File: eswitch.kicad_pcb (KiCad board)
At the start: 4 copper layers, 181 x 57.5 mm, 160 parts, among them J1 691218410002, J10 691218410002, J11 691218410002, J12 691218410002, J2 +12V IN, J3 GND IN, J4 USB-C, J5 UART, J6 691218410002, J7 691218410002, J8 691218410002, J9 691218410002, SW1 RESET, SW2 BOOT, U1 BTS7004-1EPP, U10 ESP32-S3-WROOM-1-N8, U11 SRV05-4HTG-D, U2 BTS7004-1EPP, U3 BTS7008-1EPR, U4 BTS7008-1EPR, U5 BTS7008-1EPR, U6 BTS7008-1EPR, U7 BTS7008-1EPR, U8 BTS7002-1EPP, U9 TPS54360B

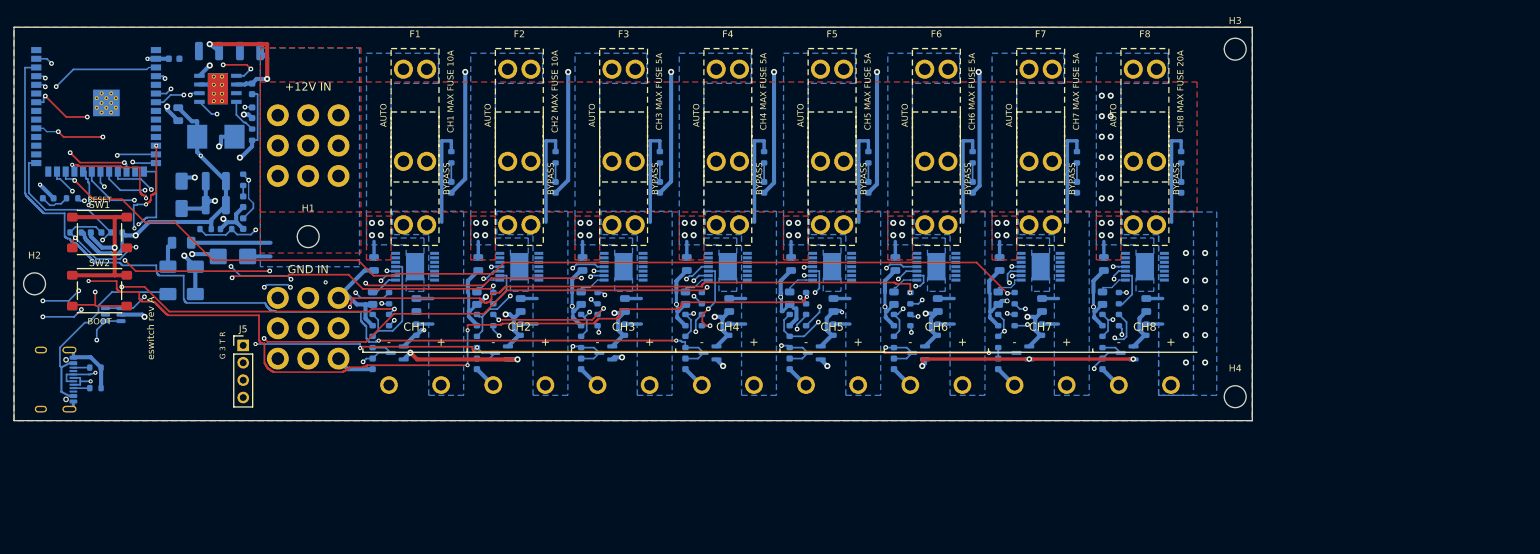
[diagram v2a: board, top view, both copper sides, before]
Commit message: Checkpoint unfinished revision B power protection and PCB review
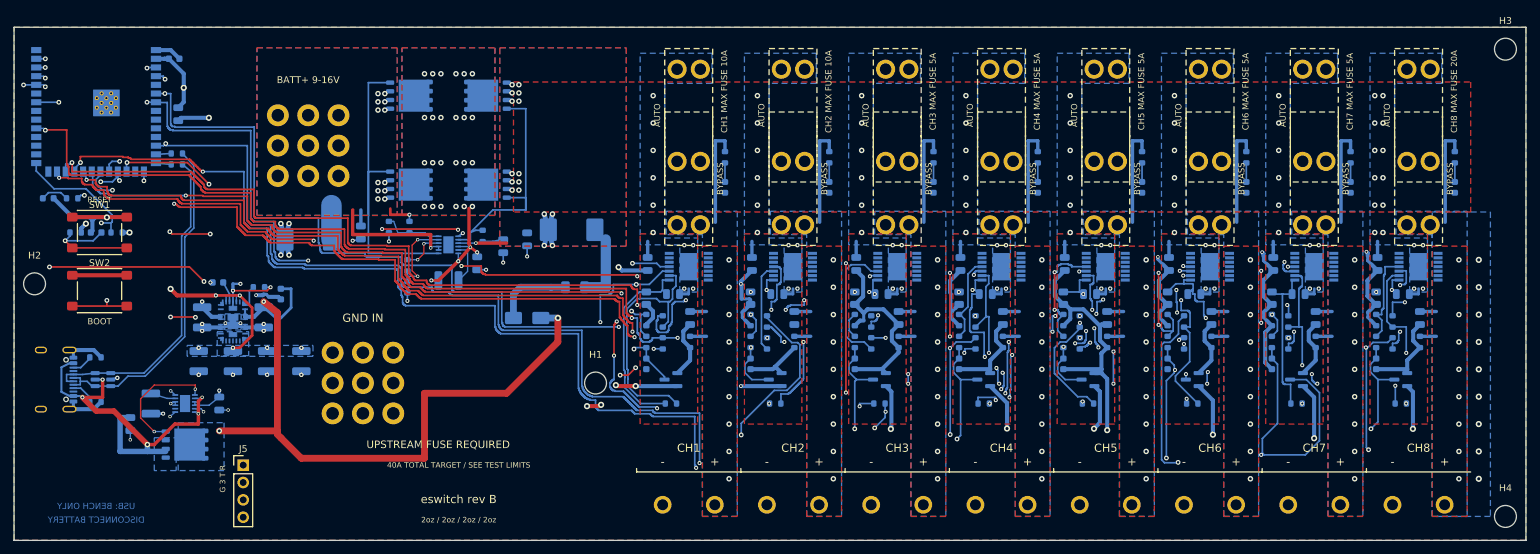
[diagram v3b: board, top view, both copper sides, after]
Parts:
- removed C4: 100nF 25V, Capacitor_SMD:C_0603_1608Metric
- removed C5: 27nF, Capacitor_SMD:C_0603_1608Metric
- removed C6: 150pF, Capacitor_SMD:C_0603_1608Metric
- removed D2, D4: B360A, Diode_SMD:D_SMA
- removed L1: 10uH 4A, Inductor_SMD:L_Bourns_SRP7028A_7.3x6.6mm
- removed R2: 31.6k 1%, Resistor_SMD:R_0603_1608Metric
- removed R3: 10.2k 1%, Resistor_SMD:R_0603_1608Metric
- removed R4: 3.9k, Resistor_SMD:R_0603_1608Metric
- added C104: 47nF 50V, Capacitor_SMD:C_0805_2012Metric, B.Cu at (96.3, 39.0)
- added C12: 22uF 10V, Capacitor_SMD:C_1210_3225Metric, B.Cu at (37.0, 48.8)
- added C13: 22uF 10V, Capacitor_SMD:C_1210_3225Metric, B.Cu at (42.0, 48.8)
- added C14: 1uF, Capacitor_SMD:C_0603_1608Metric, B.Cu at (29.8, 37.3)
- added C15: 100nF 50V, Capacitor_SMD:C_0805_2012Metric, B.Cu at (50.7, 30.0)
- added C16: 100nF 50V, Capacitor_SMD:C_0805_2012Metric, B.Cu at (67.7, 34.5)
- added C17: 4.7uF 50V, Capacitor_SMD:C_1210_3225Metric, B.Cu at (63.5, 37.0)
- added C18: 10nF 50V, Capacitor_SMD:C_0805_2012Metric, B.Cu at (71.5, 32.0)
- added C19: 100nF 50V, Capacitor_SMD:C_0805_2012Metric, B.Cu at (75.0, 31.0)
- added C20: 100nF 50V, Capacitor_SMD:C_0805_2012Metric, B.Cu at (17.0, 58.0)
- added C204: 47nF 50V, Capacitor_SMD:C_0805_2012Metric, B.Cu at (111.6, 39.0)
- added C21: 100nF 50V, Capacitor_SMD:C_0805_2012Metric, B.Cu at (30.0, 55.0)
- added C22: 4.7uF 50V, Capacitor_SMD:C_1210_3225Metric, B.Cu at (20.0, 55.0)
- added C304: 47nF 50V, Capacitor_SMD:C_0805_2012Metric, B.Cu at (126.8, 39.0)
- added C404: 47nF 50V, Capacitor_SMD:C_0805_2012Metric, B.Cu at (142.0, 39.0)
- added C504: 47nF 50V, Capacitor_SMD:C_0805_2012Metric, B.Cu at (157.3, 39.0)
- added C604: 47nF 50V, Capacitor_SMD:C_0805_2012Metric, B.Cu at (172.5, 39.0)
- added C704: 47nF 50V, Capacitor_SMD:C_0805_2012Metric, B.Cu at (187.8, 39.0)
- added C804: 47nF 50V, Capacitor_SMD:C_0805_2012Metric, B.Cu at (203.0, 39.0)
- added D6: SMCJ16A, Diode_SMD:D_SMC, B.Cu at (81.5, 29.6)
- added NT1: AGND STAR, NetTie:NetTie-2_SMD_Pad0.5mm, B.Cu at (32.0, 38.0)
- added Q1: BSC016N06NS, Package_SON:Infineon_PG-TDSON-8_6.15x5.15mm, B.Cu at (57.8, 10.0)
- added Q2: BSC016N06NS, Package_SON:Infineon_PG-TDSON-8_6.15x5.15mm, B.Cu at (57.8, 23.0)
- added Q3: BSC016N06NS, Package_SON:Infineon_PG-TDSON-8_6.15x5.15mm, B.Cu at (69.2, 10.0)
- added Q4: BSC016N06NS, Package_SON:Infineon_PG-TDSON-8_6.15x5.15mm, B.Cu at (69.2, 23.0)
- added Q5: BSC016N06NS, Package_SON:Infineon_PG-TDSON-8_6.15x5.15mm, B.Cu at (25.0, 61.0)
- added R10: 22R, Resistor_SMD:R_0603_1608Metric, B.Cu at (23.8, 20.1)
- added R108: 47k, Resistor_SMD:R_0603_1608Metric, B.Cu at (96.0, 55.0)
- added R11: 22R, Resistor_SMD:R_0603_1608Metric, B.Cu at (23.8, 18.4)
- added R12: 127k 0.1%, Resistor_SMD:R_0603_1608Metric, B.Cu at (57.5, 34.8)
- added R13: 10k 0.1%, Resistor_SMD:R_0603_1608Metric, B.Cu at (57.5, 38.0)
- added R14: 59k 0.1%, Resistor_SMD:R_0603_1608Metric, B.Cu at (57.8, 29.2)
- added R15: 10k 0.1%, Resistor_SMD:R_0603_1608Metric, B.Cu at (54.8, 29.2)
- added R16: 100R, Resistor_SMD:R_0603_1608Metric, B.Cu at (68.5, 30.5)
- added R208: 47k, Resistor_SMD:R_0603_1608Metric, B.Cu at (111.3, 55.0)
- added R308: 47k, Resistor_SMD:R_0603_1608Metric, B.Cu at (126.5, 55.0)
- added R408: 47k, Resistor_SMD:R_0603_1608Metric, B.Cu at (141.7, 55.0)
- added R508: 47k, Resistor_SMD:R_0603_1608Metric, B.Cu at (157.0, 55.0)
- added R608: 47k, Resistor_SMD:R_0603_1608Metric, B.Cu at (172.2, 55.0)
- added R708: 47k, Resistor_SMD:R_0603_1608Metric, B.Cu at (187.5, 55.0)
- added R808: 47k, Resistor_SMD:R_0603_1608Metric, B.Cu at (202.7, 55.0)
- added U12: LM74800-Q1, Package_SON:WSON-12-1EP_3x3mm_P0.5mm_EP1.5x2.5mm, B.Cu at (63.5, 31.8)
- added U13: LM74800-Q1, Package_SON:WSON-12-1EP_3x3mm_P0.5mm_EP1.5x2.5mm, B.Cu at (25.0, 55.0)
- D3: value SMBJ26A -> SMCJ24CA; footprint Diode_SMD:D_SMB -> Diode_SMD:D_SMC
- J2: value +12V IN -> BATT+ 9-16V
- R1: value 200k 1% -> 16.5k 1%
- U9: value TPS54360B -> TPSM63603V3; footprint Package_SO:TI_SO-PowerPAD-8_ThermalVias -> eswitch:TI_RDH0030A_TPSM63603
- moved F9 57.9 mm to (82.0, 38.0)
- moved D1 51.1 mm to (75.0, 42.5)
- moved H1 47.1 mm to (85.0, 52.0)
- moved J9 43.7 mm to (155.8, 69.8)
- moved J1 43.7 mm to (94.8, 69.8)
- moved J10 43.7 mm to (171.0, 69.8)
- moved J11 43.7 mm to (186.2, 69.8)
- moved J12 43.7 mm to (201.5, 69.8)
- moved J6 43.7 mm to (110.0, 69.8)
- moved J7 43.7 mm to (125.3, 69.8)
- moved J8 43.7 mm to (140.5, 69.8)
- moved H4 43.2 mm to (218.0, 71.5)
- moved D401 40.2 mm to (141.7, 51.5)
- moved D201 40.2 mm to (111.3, 51.5)
- moved D301 40.2 mm to (126.5, 51.5)
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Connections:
- D3 pad 1: +12V -> /BATT_RAW
- J2 pad 1: +12V -> /BATT_RAW
- R1 pad 2: GND -> /AGND_BUCK
- U10 pad 13: /USB_D- -> /USB_MCU_D-
- U10 pad 14: /USB_D+ -> /USB_MCU_D+
- U9 pad 1: /BOOT -> /RT
- U9 pad 3: (no net) -> /VIN
- U9 pad 4: /RT -> /VIN
- U9 pad 5: /FB -> GND
- U9 pad 6: /COMP -> GND
- U9 pad 7: GND -> +3V3
- U9 pad 8: /SW -> +3V3
- U9 pad 9: GND -> +3V3
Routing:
- net /INR3: track 6.59 -> 115.6 mm, vias 2 -> 10
- net /DEN: track 217.2 -> 319.0 mm, vias 11 -> 12
- net +3V3: track 237.9 -> 330.7 mm, vias 11 -> 21
- net /IN3: track 92.1 -> 4.81 mm, vias 6 -> 1
- net /IS7: track 165.0 -> 248.1 mm, vias 6 -> 3
- net /IN6: track 152.6 -> 234.9 mm
- net /IS6: track 132.1 -> 209.5 mm, vias 4 -> 7
- net GND: track 390.1 -> 313.0 mm, vias 29 -> 41
- net /UGND2: track 4.40 -> 77.1 mm, vias 0 -> 6
- net /IN2: track 65.5 -> 136.6 mm, vias 3 -> 4
- net /VIN: track 73.9 -> 145.1 mm, vias 3 -> 8
- net /DENR5: track 10.3 -> 73.2 mm, vias 2 -> 4
- net /IS5: track 121.9 -> 177.7 mm, vias 2 -> 3
- net /DENR4: track 11.7 -> 67.3 mm, vias 2 -> 8
- net /FB: track 54.5 -> 0.00 mm, vias 2 -> 0
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- added copper zone on B.Cu, net +3V3
- added copper zone on B.Cu, net /BATT_MID
- added copper zone on F.Cu, net /BATT_MID
- added copper zone on In2.Cu, net /BATT_MID
- added copper zone on B.Cu, net /BATT_RAW
- added copper zone on F.Cu, net /BATT_RAW
- added copper zone on In2.Cu, net /BATT_RAW
- added copper zone on F.Cu, net /LOAD1
- added copper zone on F.Cu, net /LOAD2
- added copper zone on F.Cu, net /LOAD3
- added copper zone on F.Cu, net /LOAD4
- added copper zone on F.Cu, net /LOAD5
- added copper zone on F.Cu, net /LOAD6
- added copper zone on F.Cu, net /LOAD7
- added copper zone on F.Cu, net /LOAD8
- added copper zone on B.Cu, net /VIN
- added copper zone on B.Cu, net VBUS
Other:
- board size 181 x 57.5 mm -> 221 x 75 mm
- board text added: "2oz / 2oz / 2oz / 2oz"
- board text added: "40A TOTAL TARGET / SEE TEST LIMITS"
- board text added: "BATT+ 9-16V"
- board text added: "DISCONNECT BATTERY"
- board text added: "UPSTREAM FUSE REQUIRED"
- board text added: "USB: BENCH ONLY"
- board text added: "eswitch rev B"
- board text removed: "+12V IN"
- board text removed: "USB"
- board text removed: "eswitch rev A"
- board text removed: "eswitch rev A - SMD side"
